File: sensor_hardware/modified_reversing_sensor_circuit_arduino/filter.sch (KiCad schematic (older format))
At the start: 32 parts, among them Q6 2SC1623-L6, U1001 LM6132, U2 NE5532

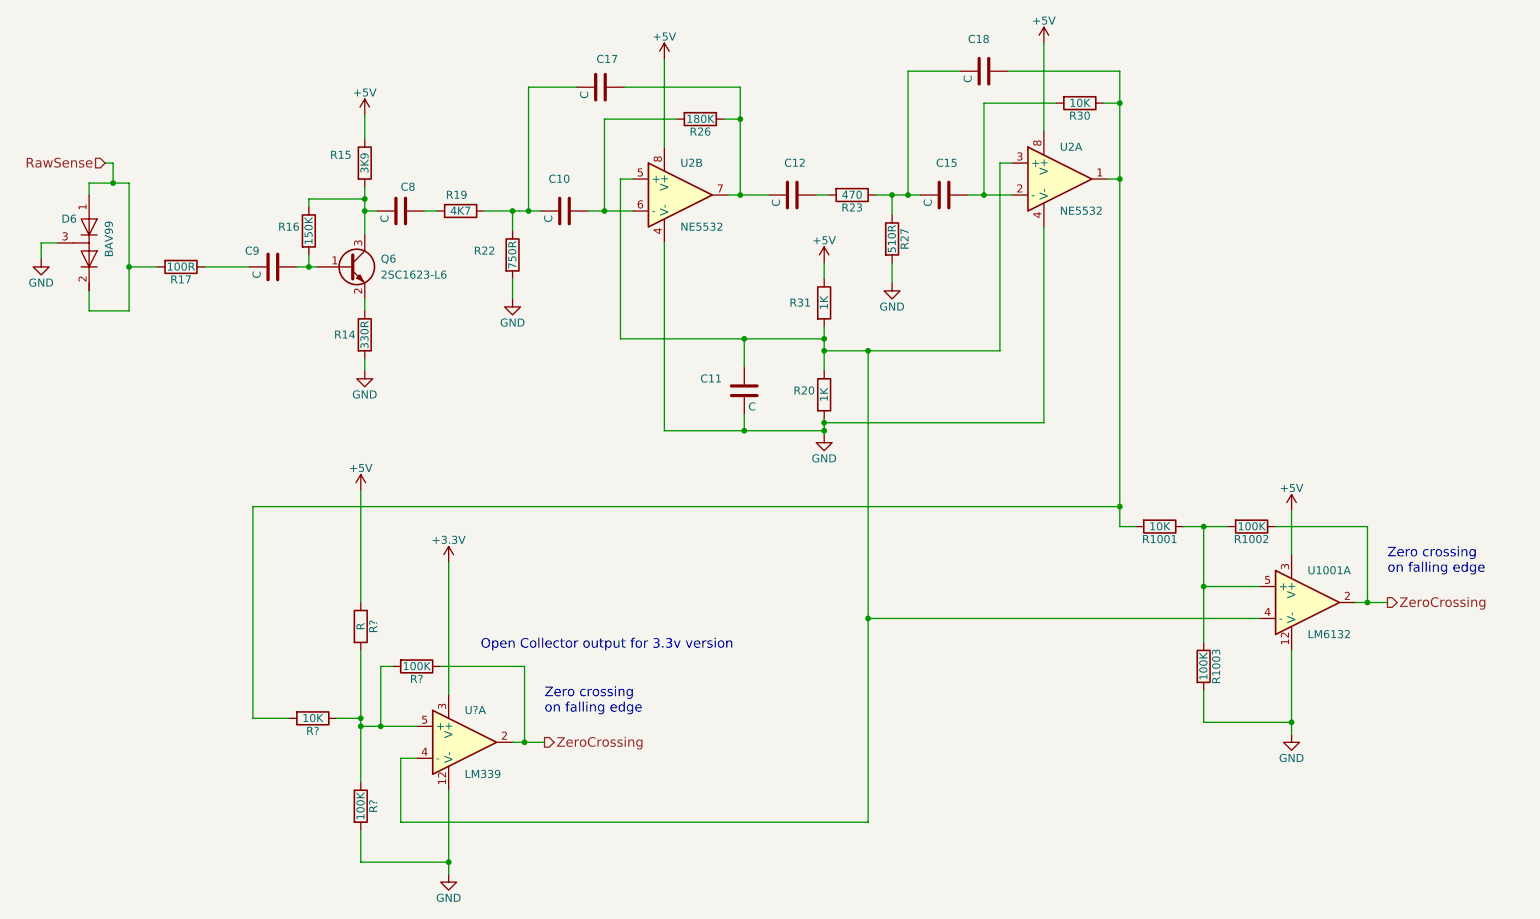
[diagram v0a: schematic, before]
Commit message: make specific atmega328 version
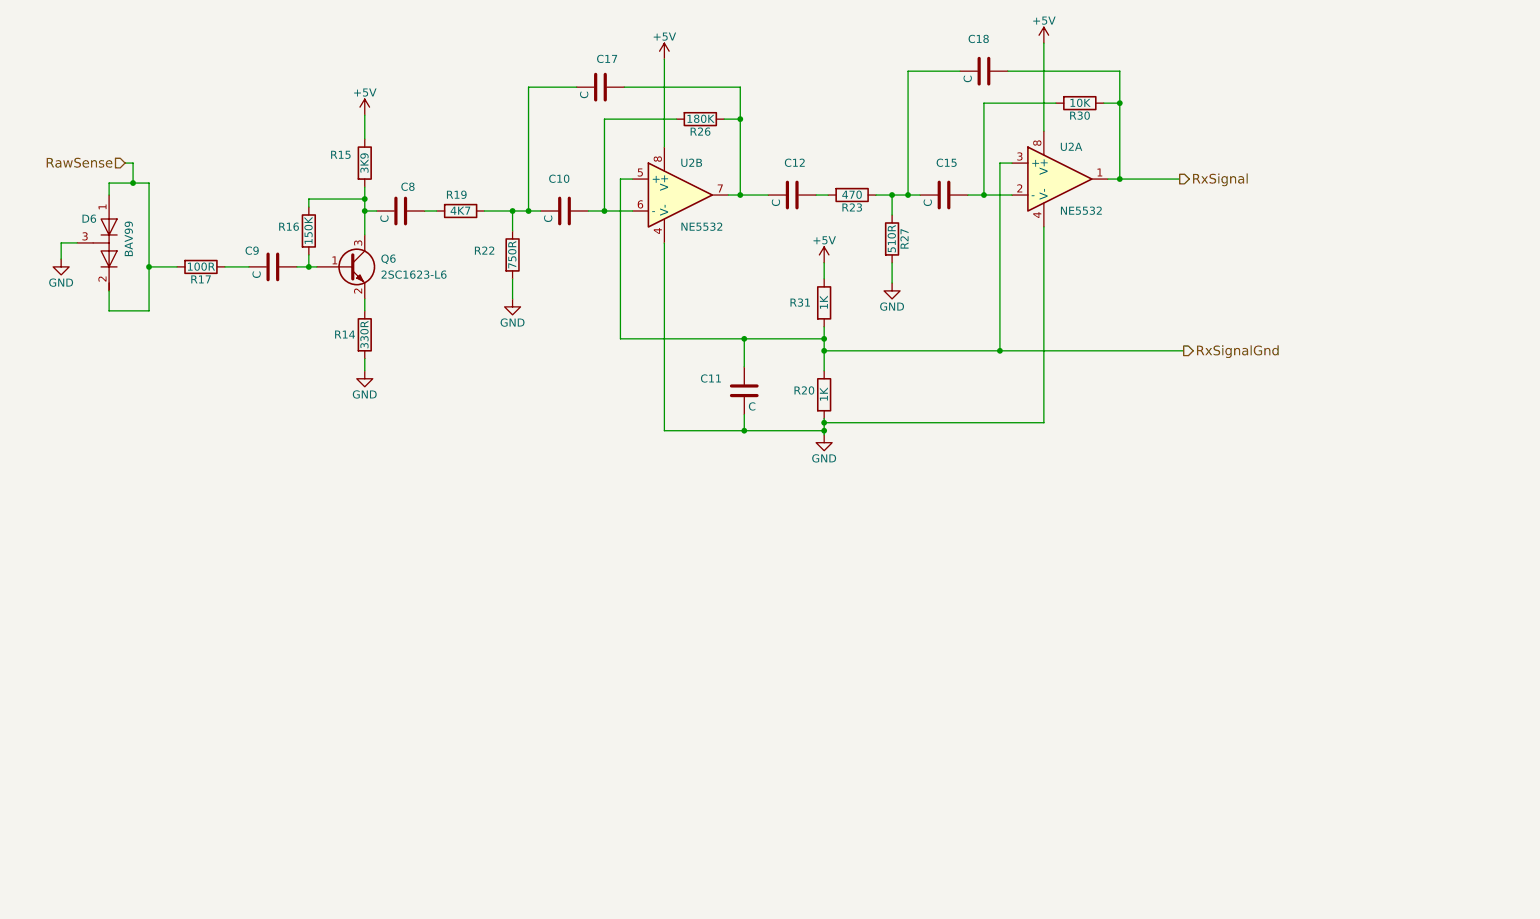
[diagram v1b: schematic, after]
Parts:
- removed R1001, R?: 10K, symbol R
- removed R1002, R1003, R? (x2): 100K, symbol R
- removed R?: R, symbol R
- removed U1001: LM6132, symbol LM339
- removed U?: LM339, symbol LM339
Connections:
- net RxSignalGnd: now reaches C11.1, R20.1, R31.2, U2.3 (+), U2.5 (+)
- net RxSignal: now reaches C18.1, R30.1, U2.1
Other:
- note removed: "Open Collector output for 3.3v version"
- note removed: "Zero crossing \non falling edge"
- moved on the sheet: D6, R17

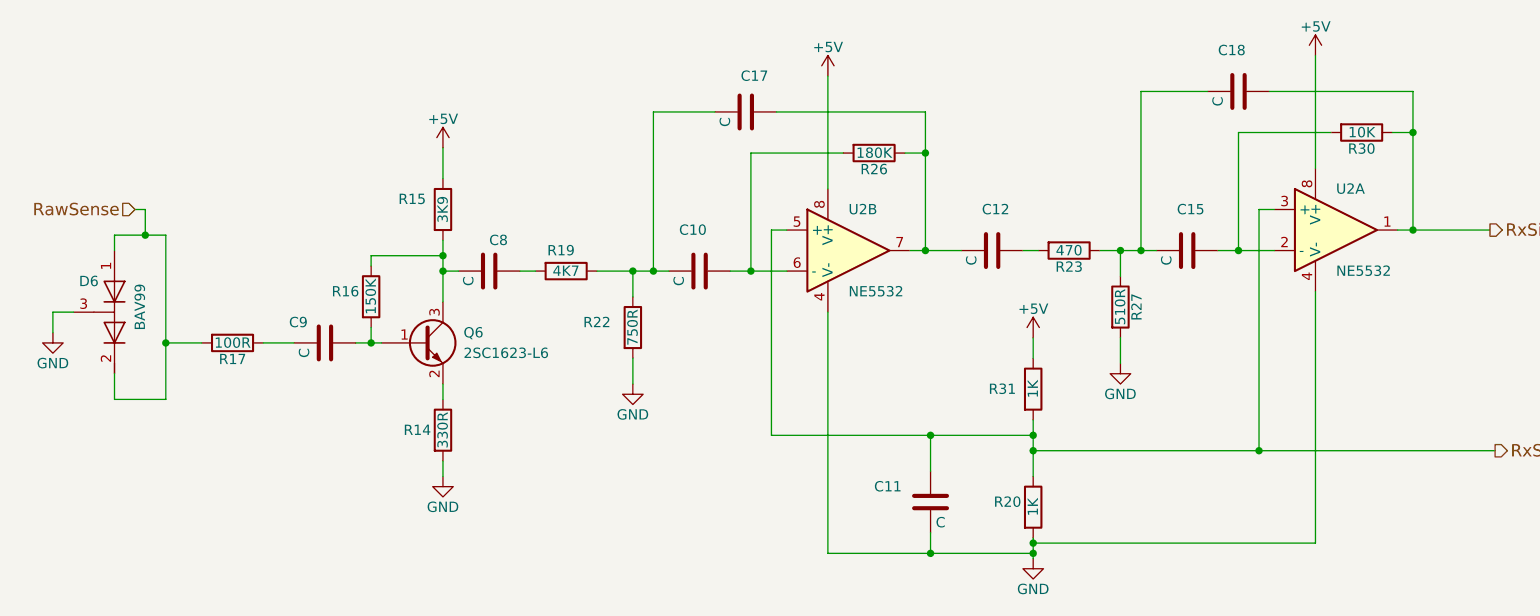
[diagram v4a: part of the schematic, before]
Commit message: update readme and add wifi circuit details
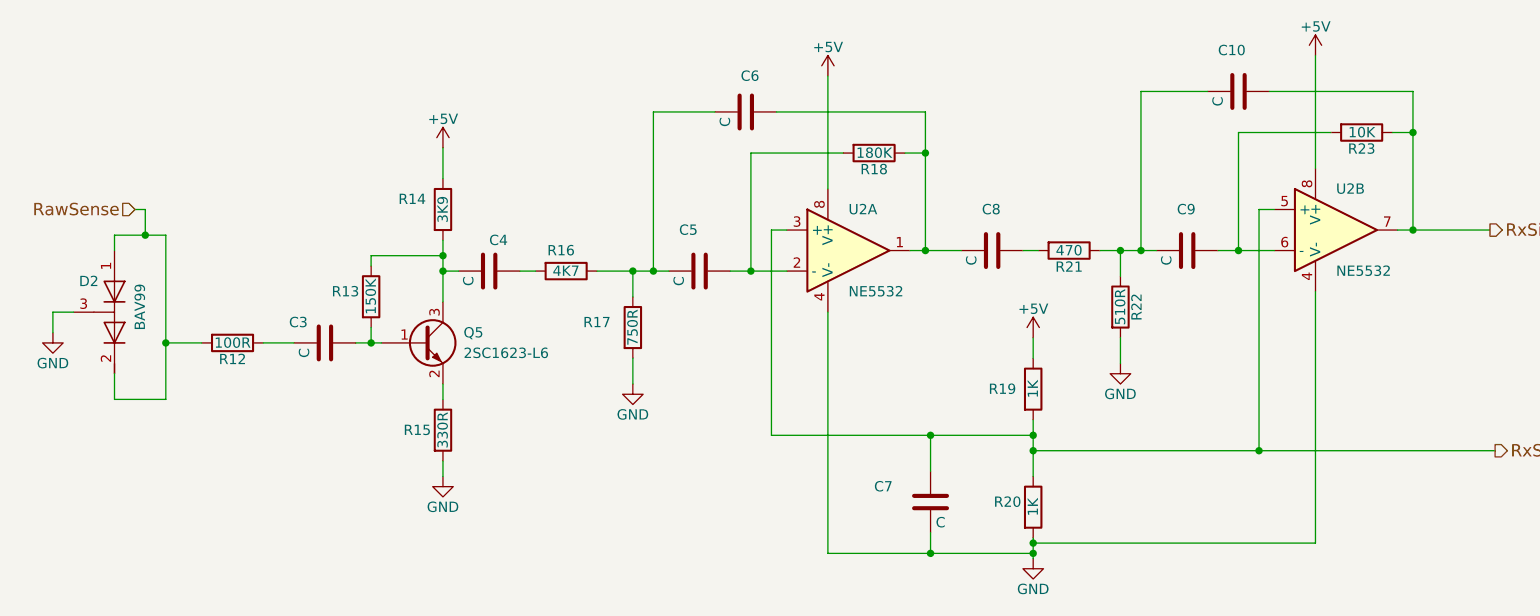
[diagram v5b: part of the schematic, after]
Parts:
- renumbered C18 to C10, C9 to C3, C8 to C4, C10 to C5, C17 to C6, C11 to C7, C12 to C8, C15 to C9, D6 to D2, Q6 to Q5, R17 to R12, R16 to R13, R15 to R14, R14 to R15, R19 to R16, R22 to R17, R26 to R18, R31 to R19, R23 to R21, R27 to R22, R30 to R23
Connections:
- net RxSignal: now also U2.7; no longer U2.1
- net RxSignalGnd: now also U2.3 (+), U2.5 (+); no longer U2.3 (+), U2.5 (+)
- net at C5.1, R18.2: now also U2.2 (-); no longer U2.6 (-)
- net at C6.1, C8.2, R18.1: now also U2.1; no longer U2.7
- net at C9.1, R23.2: now also U2.6 (-); no longer U2.2 (-)
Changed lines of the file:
@@
 LIBS:valves
 LIBS:atmega328p
+LIBS:esp-01
 LIBS:reversing_sensor_circuit-cache
 EELAYER 25 0
@@
 $Descr A4 11693 8268
 encoding utf-8
-Sheet 3 4
+Sheet 3 5
 Title ""
 Date ""
@@
 $EndComp
 $Comp
-L R R14
+L R R15
 U 1 1 607437D5
 P 3500 3475
-F 0 "R14" H 3375 3475 50  0000 C CNN
+F 0 "R15" H 3375 3475 50  0000 C CNN
 F 1 "330R" V 3500 3475 50  0000 C CNN
 F 2 "" V 3430 3475 50  0001 C CNN
@@
 $EndComp
 $Comp
-L C C9
+L C C3
 U 1 1 607437DC
 P 2925 3050
-F 0 "C9" V 2825 2875 50  0000 L CNN
+F 0 "C3" V 2825 2875 50  0000 L CNN
 F 1 "C" H 2950 2950 50  0000 L CNN
 F 2 "" H 2963 2900 50  0001 C CNN
@@
 	3075 3050 3200 3050
 $Comp
-L R R16
+L R R13
 U 1 1 607437E7
 P 3150 2825
-F 0 "R16" H 3025 2850 50  0000 C CNN
+F 0 "R13" H 3025 2850 50  0000 C CNN
 F 1 "150K" V 3150 2825 50  0000 C CNN
 F 2 "" V 3080 2825 50  0001 C CNN
@@
 $EndComp
 $Comp
-L R R15
+L R R14
 U 1 1 607437EE
 P 3500 2400
-F 0 "R15" H 3350 2450 50  0000 C CNN
+F 0 "R14" H 3350 2450 50  0000 C CNN
 F 1 "3K9" V 3500 2400 50  0000 C CNN
 F 2 "" V 3430 2400 50  0001 C CNN
@@
 	3500 2250 3500 2100
 $Comp
-L R R17
+L R R12
 U 1 1 60743804
 P 2475 3050
-F 0 "R17" V 2555 3050 50  0000 C CNN
+F 0 "R12" V 2555 3050 50  0000 C CNN
 F 1 "100R" V 2475 3050 50  0000 C CNN
 F 2 "" V 2405 3050 50  0001 C CNN
@@
 $EndComp
 $Comp
-L R R19
+L R R16
 U 1 1 6074380B
 P 4100 2700
-F 0 "R19" V 4000 2675 50  0000 C CNN
+F 0 "R16" V 4000 2675 50  0000 C CNN
 F 1 "4K7" V 4100 2700 50  0000 C CNN
 F 2 "" V 4030 2700 50  0001 C CNN
@@
 $EndComp
 $Comp
-L C C8
+L C C4
 U 1 1 60743812
 P 3725 2700
-F 0 "C8" V 3575 2700 50  0000 L CNN
+F 0 "C4" V 3575 2700 50  0000 L CNN
 F 1 "C" H 3750 2600 50  0000 L CNN
 F 2 "" H 3763 2550 50  0001 C CNN
@@
 $EndComp
 $Comp
-L R R31
+L R R19
 U 1 1 60743819
 P 6375 3275
-F 0 "R31" H 6225 3275 50  0000 C CNN
+F 0 "R19" H 6225 3275 50  0000 C CNN
 F 1 "1K" V 6375 3275 50  0000 C CNN
 F 2 "" V 6305 3275 50  0001 C CNN
@@
 $Comp
 L LM358 U2
-U 2 1 60743838
+U 1 1 60743838
 P 5475 2600
 F 0 "U2" H 5475 2800 50  0000 L CNN
@@
 F 2 "" H 5475 2600 50  0001 C CNN
 F 3 "" H 5475 2600 50  0001 C CNN
-	2    5475 2600
-	1    0    0    -1
-$EndComp
-$Comp
-L R R22
+	1    5475 2600
+	1    0    0    -1
+$EndComp
+$Comp
+L R R17
 U 1 1 6074383F
 P 4425 2975
-F 0 "R22" H 4250 3000 50  0000 C CNN
+F 0 "R17" H 4250 3000 50  0000 C CNN
 F 1 "750R" V 4425 2975 50  0000 C CNN
 F 2 "" V 4355 2975 50  0001 C CNN
@@
 	4425 3250 4425 3125
 $Comp
-L R R26
+L R R18
 U 1 1 6074384F
 P 5600 2125
-F 0 "R26" V 5680 2125 50  0000 C CNN
+F 0 "R18" V 5680 2125 50  0000 C CNN
 F 1 "180K" V 5600 2125 50  0000 C CNN
 F 2 "" V 5530 2125 50  0001 C CNN
@@
 $EndComp
 $Comp
-L C C17
+L C C6
 U 1 1 60743856
 P 4975 1925
-F 0 "C17" V 4800 1900 50  0000 L CNN
+F 0 "C6" V 4800 1900 50  0000 L CNN
 F 1 "C" H 5000 1825 50  0000 L CNN
 F 2 "" H 5013 1775 50  0001 C CNN
@@
 $EndComp
 $Comp
-L C C10
+L C C5
 U 1 1 6074385D
 P 4750 2700
-F 0 "C10" V 4550 2600 50  0000 L CNN
+F 0 "C5" V 4550 2600 50  0000 L CNN
 F 1 "C" H 4775 2600 50  0000 L CNN
 F 2 "" H 4788 2550 50  0001 C CNN
@@
 Connection ~ 4525 2700
 $Comp
-L R R23
+L R R21
 U 1 1 60743878
 P 6550 2600
-F 0 "R23" V 6630 2600 50  0000 C CNN
+F 0 "R21" V 6630 2600 50  0000 C CNN
 F 1 "470" V 6550 2600 50  0000 C CNN
 F 2 "" V 6480 2600 50  0001 C CNN
@@
 $EndComp
 $Comp
-L C C12
+L C C8
 U 1 1 6074387F
 P 6175 2600
-F 0 "C12" V 5975 2550 50  0000 L CNN
+F 0 "C8" V 5975 2550 50  0000 L CNN
 F 1 "C" H 6200 2500 50  0000 L CNN
 F 2 "" H 6213 2450 50  0001 C CNN
@@
 $Comp
 L LM358 U2
-U 1 1 60743886
+U 2 1 60743886
 P 7850 2500
 F 0 "U2" H 7850 2700 50  0000 L CNN
@@
 F 2 "" H 7850 2500 50  0001 C CNN
 F 3 "" H 7850 2500 50  0001 C CNN
-	1    7850 2500
-	1    0    0    -1
-$EndComp
-$Comp
-L R R27
+	2    7850 2500
+	1    0    0    -1
+$EndComp
+$Comp
+L R R22
 U 1 1 6074388D
 P 6800 2875
-F 0 "R27" V 6880 2875 50  0000 C CNN
+F 0 "R22" V 6880 2875 50  0000 C CNN
 F 1 "510R" V 6800 2875 50  0000 C CNN
 F 2 "" V 6730 2875 50  0001 C CNN
@@
 	6800 3150 6800 3025
 $Comp
-L R R30
+L R R23
 U 1 1 6074389D
 P 7975 2025
-F 0 "R30" V 8055 2025 50  0000 C CNN
+F 0 "R23" V 8055 2025 50  0000 C CNN
 F 1 "10K" V 7975 2025 50  0000 C CNN
 F 2 "" V 7905 2025 50  0001 C CNN
@@
 $EndComp
 $Comp
-L C C18
+L C C10
 U 1 1 607438A4
 P 7375 1825
-F 0 "C18" V 7175 1725 50  0000 L CNN
+F 0 "C10" V 7175 1725 50  0000 L CNN
 F 1 "C" H 7400 1725 50  0000 L CNN
 F 2 "" H 7413 1675 50  0001 C CNN
@@
 $EndComp
 $Comp
-L C C15
+L C C9
 U 1 1 607438AB
 P 7125 2600
-F 0 "C15" V 6925 2550 50  0000 L CNN
+F 0 "C9" V 6925 2550 50  0000 L CNN
 F 1 "C" H 7150 2500 50  0000 L CNN
 F 2 "" H 7163 2450 50  0001 C CNN
@@
 Connection ~ 3500 2700
 $Comp
-L D_x2_Serial_AKC D6
+L D_x2_Serial_AKC D2
 U 1 1 60743912
 P 1900 2900
-F 0 "D6" V 1750 2775 50  0000 C CNN
+F 0 "D2" V 1750 2775 50  0000 C CNN
 F 1 "BAV99" H 1875 3025 50  0000 C CNN
 F 2 "" H 1900 2900 50  0001 C CNN
@@
 Connection ~ 6375 3500
 $Comp
-L Q_NPN_BEC Q6
+L Q_NPN_BEC Q5
 U 1 1 60743939
 P 3400 3050
-F 0 "Q6" H 3600 3100 50  0000 L CNN
+F 0 "Q5" H 3600 3100 50  0000 L CNN
 F 1 "2SC1623-L6" H 3600 3000 50  0000 L CNN
 F 2 "" H 3600 3150 50  0001 C CNN
@@
 Connection ~ 5850 2125
 $Comp
-L C C11
+L C C7
 U 1 1 60737A5C
 P 5875 3825
-F 0 "C11" H 5600 3900 50  0000 L CNN
+F 0 "C7" H 5600 3900 50  0000 L CNN
 F 1 "C" H 5900 3725 50  0000 L CNN
 F 2 "" H 5913 3675 50  0001 C CNN
